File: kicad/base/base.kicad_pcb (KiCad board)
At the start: 2 copper layers, 63 x 50 mm, 23 parts, among them J1 TO ARM, Q1 MMBT3904, Q2 MMBT3904, Q3 MMBT3904, SW2 SW_SPST_LED_RGB, U1 Seeeduiono_Xiao, U2 NC7SB3257P6X, U3 AS5600

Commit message: something
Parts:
- added REF**: JLCPCB Tooling Hole, base:JLCPCB Tooling Hole, F.Cu at (158.0, 73.0)
- added REF**: JLCPCB Tooling Hole, base:JLCPCB Tooling Hole, F.Cu at (126.0, 119.0)
- added REF**: JLCPCB Tooling Hole, base:JLCPCB Tooling Hole, F.Cu at (158.0, 119.0)
- R5: value 65R -> 68R
- moved R6 42.1 mm to (158.3, 102.0), turned to 270 degrees
- moved Q1 35.9 mm to (154.8, 102.0), turned to 0 degrees
- moved R8 30.1 mm to (151.3, 102.0), turned to 90 degrees
- moved U2 27.7 mm to (133.0, 78.0)
- moved R5 26.0 mm to (133.1, 111.3), turned to 270 degrees
- moved R3 23.6 mm to (145.0, 78.0), turned to 270 degrees
- moved Q2 23.5 mm to (129.6, 111.3), turned to 0 degrees
- moved R9 22.8 mm to (126.1, 111.3), turned to 90 degrees
- moved R2 22.0 mm to (142.0, 78.0)
- moved R1 18.9 mm to (139.0, 78.0), turned to 270 degrees
- moved R7 18.0 mm to (133.1, 106.3), turned to 270 degrees
- moved U1 17.2 mm to (128.0, 92.0), turned to 270 degrees
- moved J1 14.2 mm to (145.0, 88.0), turned to 180 degrees
- moved Q3 14.0 mm to (129.6, 106.3), turned to 0 degrees
- moved R10 12.9 mm to (126.1, 106.3), turned to 90 degrees
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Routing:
- net SDA1: track 15.6 -> 58.5 mm
- net G_CONT: track 7.13 -> 25.9 mm, vias 0 -> 2
- net Net-(R5-Pad1): track 26.3 -> 8.06 mm, vias 2 -> 0
- net +3V3: track 127.4 -> 145.1 mm, vias 2 -> 1
- net Net-(R7-Pad1): track 37.3 -> 20.6 mm
- net SCL: track 49.5 -> 61.2 mm, vias 3 -> 1
- net SDA2: track 29.1 -> 18.6 mm, vias 0 -> 2
- net SEL: track 16.8 -> 9.06 mm, vias 2 -> 0
- net EN_SW: track 28.8 -> 21.5 mm, vias 0 -> 2
- net R_CONT: track 9.73 -> 16.0 mm
- net Net-(R6-Pad1): track 31.4 -> 37.3 mm, vias 2 -> 0
- net GND: track 1.30 -> 3.49 mm, vias 35 -> 33
- net B_CONT: track 12.2 -> 10.5 mm
- net SDA: track 23.5 -> 24.4 mm
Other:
- outline, holes or cut-outs redrawn

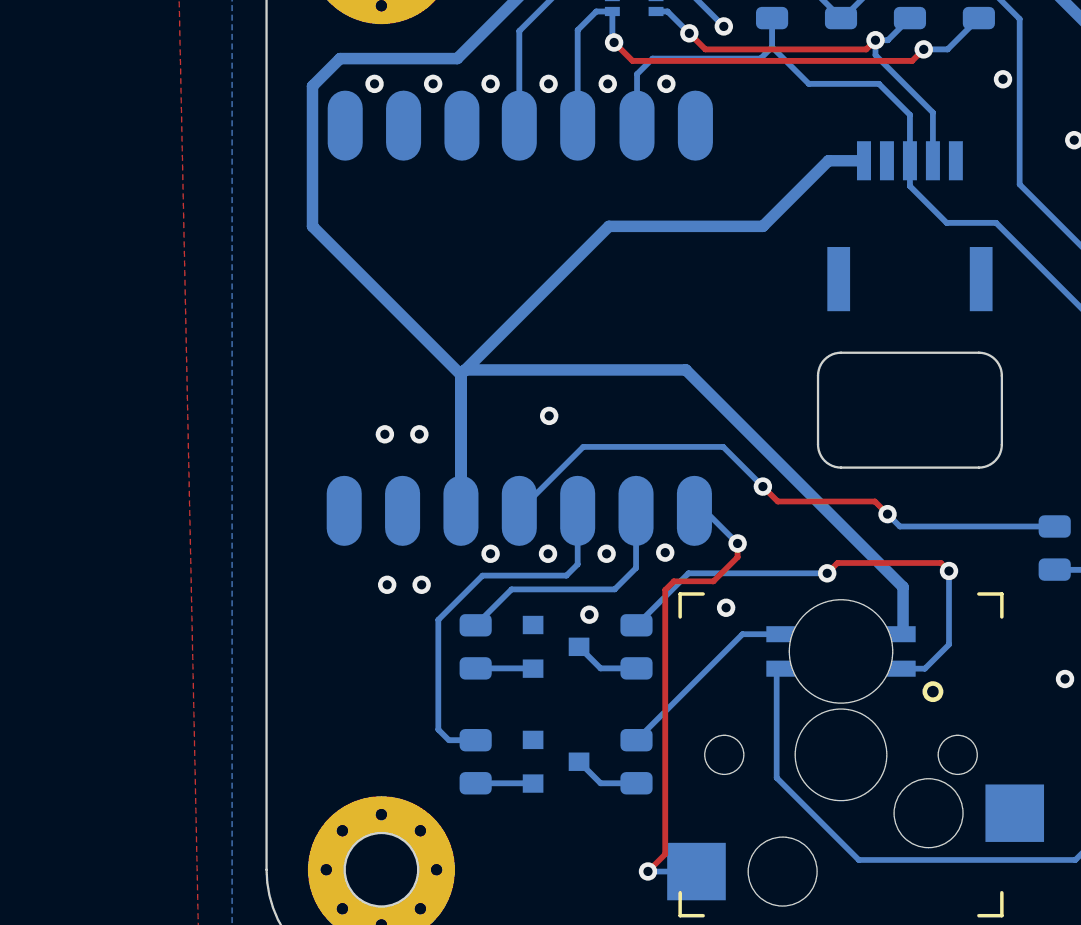
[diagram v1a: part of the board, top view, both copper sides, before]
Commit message: added left hand support, updated pcb with logo, updated pen geometry
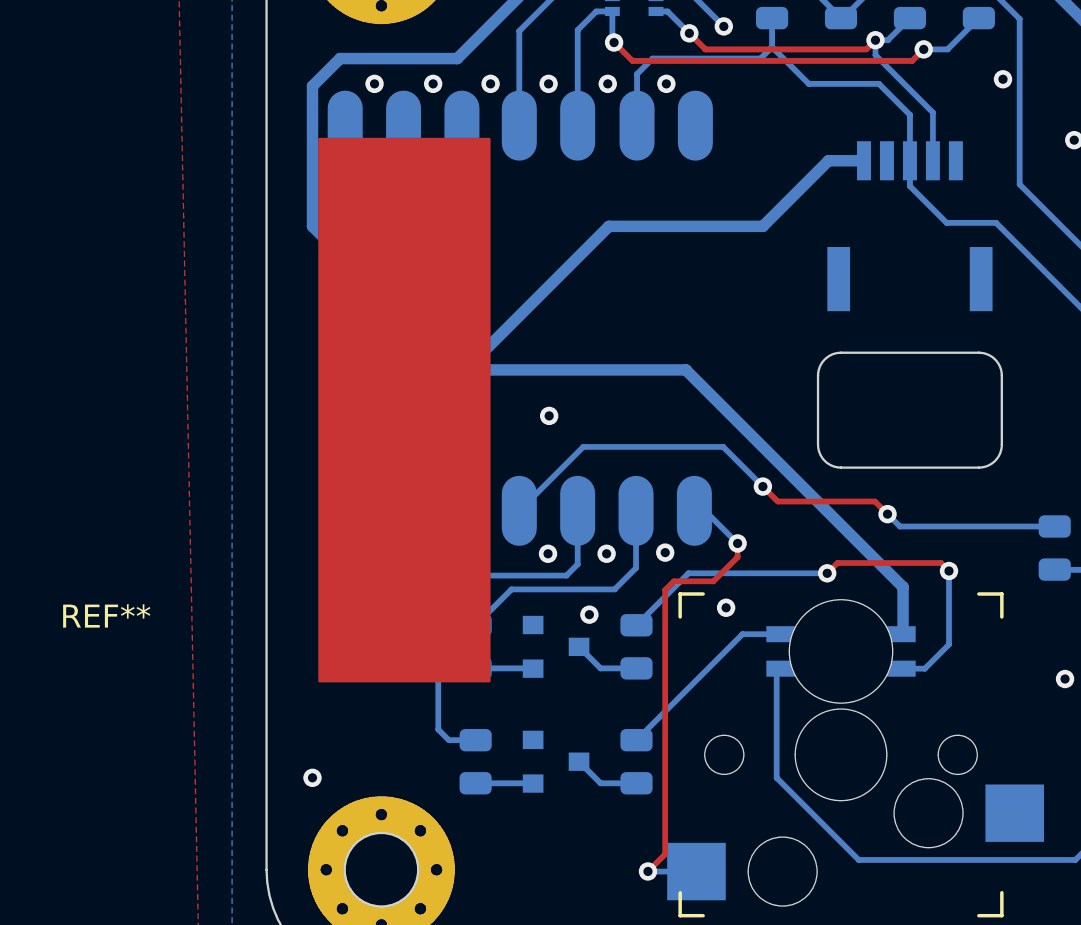
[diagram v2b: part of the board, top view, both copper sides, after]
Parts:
- added G***: LOGO, base:hyku_logo, F.Cu at (123.0, 96.0)
- added REF**: hyku_logo, base:hyku_logo, F.Cu at (0.00, 0.00)
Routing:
- net GND: vias 33 -> 29
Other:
- board text added: "v1.1"
